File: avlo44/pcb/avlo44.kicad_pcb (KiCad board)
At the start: 2 copper layers, 356.5 x 105.3 mm, 102 parts, among them P1 OLED, SW1 SW_PUSH, SW10 SW_PUSH, SW11 SW_PUSH, SW12 SW_PUSH, SW13 SW_PUSH, SW14 SW_PUSH, SW15 SW_PUSH, SW16 SW_PUSH, SW17 SW_PUSH, SW18 SW_PUSH, SW19 SW_PUSH, SW2 SW_PUSH, SW20 SW_PUSH, SW21 SW_PUSH, SW22 SW_PUSH, SW25 SW_PUSH, SW26 SW_PUSH, SW27 SW_PUSH, SW28 SW_PUSH, SW29 SW_PUSH, SW3 SW_PUSH, SW30 SW_PUSH, SW31 SW_PUSH, SW32 SW_PUSH, SW33 SW_PUSH, SW34 SW_PUSH, SW35 SW_PUSH, SW36 SW_PUSH, SW37 SW_PUSH, SW38 SW_PUSH, SW39 SW_PUSH, SW4 SW_PUSH, SW40 SW_PUSH, SW41 SW_PUSH, SW42 SW_PUSH, SW43 SW_PUSH, SW44 SW_PUSH, SW45 SW_PUSH, SW46 SW_PUSH, SW5 SW_PUSH, SW6 SW_PUSH, SW7 SW_PUSH, SW8 SW_PUSH, SW9 SW_PUSH, U1 ProMicro

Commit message: Initial routing complete for Avlo44
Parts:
- removed L11: WS2812B, avlo-parts:WS2812B
- moved L7 4.90 mm to (317.1, -205.1)
- moved L8 2.64 mm to (331.7, -227.2)
- moved L10 1.47 mm to (272.9, -227.2)
- moved L9 0.72 mm to (310.3, -234.8)
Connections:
- L10 pad 2: Net-(L10-Pad2) -> (no net)
- SW37 pad 1: Net-(SW37-Pad1) -> col0
- SW38 pad 1: Net-(SW38-Pad1) -> col1
- SW39 pad 1: Net-(SW39-Pad1) -> col2
- SW40 pad 1: Net-(SW40-Pad1) -> col3
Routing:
- net GND: track 327.8 -> 695.8 mm, vias 12 -> 20
- net VCC: track 278.4 -> 591.0 mm, vias 8 -> 17
- net Net-(D36-Pad2): track 2.67 -> 155.0 mm, vias 0 -> 1
- net Net-(D30-Pad2): track 2.67 -> 149.1 mm, vias 0 -> 2
- net Net-(D34-Pad2): track 0.00 -> 143.0 mm, vias 0 -> 4
- net Net-(D35-Pad2): track 2.67 -> 141.7 mm, vias 0 -> 3
- net Net-(D29-Pad2): track 0.00 -> 136.4 mm, vias 0 -> 4
- net Net-(D28-Pad2): track 0.00 -> 124.6 mm, vias 0 -> 4
- net row4: track 0.00 -> 121.6 mm, vias 0 -> 2
- net Net-(D33-Pad2): track 0.00 -> 120.7 mm, vias 0 -> 4
- net Net-(L5-Pad2): track 123.4 -> 238.0 mm, vias 2 -> 4
- net Net-(D27-Pad2): track 0.00 -> 111.6 mm, vias 0 -> 4
- net Net-(D32-Pad2): track 0.00 -> 108.7 mm, vias 0 -> 4
- net row5: track 0.00 -> 106.8 mm, vias 0 -> 2
- net Net-(D26-Pad2): track 0.00 -> 95.9 mm, vias 0 -> 2
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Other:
- board size 356.5 x 105.3 mm -> 356.5 x 105.4 mm

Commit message: Add board outline for Avlo44
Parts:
- moved D1 363.1 mm to (163.1, 133.1)
- moved D10 363.1 mm to (176.8, 145.8)
- moved D11 363.1 mm to (181.4, 145.8)
- moved D12 363.1 mm to (186.0, 145.8)
- moved D13 363.1 mm to (163.1, 158.5)
- moved D14 363.1 mm to (167.7, 158.5)
- moved D15 363.1 mm to (172.3, 158.5)
- moved D16 363.1 mm to (176.8, 158.5)
- moved D17 363.1 mm to (181.4, 158.5)
- moved D18 363.1 mm to (186.0, 158.5)
- moved D19 363.1 mm to (163.1, 171.2)
- moved D2 363.1 mm to (167.7, 133.1)
- moved D20 363.1 mm to (167.7, 171.2)
- moved D21 363.1 mm to (172.3, 171.2)
- moved D22 363.1 mm to (176.8, 171.2)
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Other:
- outline, holes or cut-outs redrawn

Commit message: Update mounting holes, add artwork and add production files
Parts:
- added ?: , avlo-parts:artwork-bicyclist, F.Cu at (238.2, 195.9)
- added ?: , avlo-parts:artwork-tireswing, B.Cu at (184.5, 192.8)
- added TH1: HOLE, avlo-parts:HOLE_M2_TH, F.Cu at (63.6, 116.1)
- added TH10: HOLE, avlo-parts:HOLE_M2_TH, F.Cu at (283.9, 190.5)
- added TH11: HOLE, avlo-parts:HOLE_M2_TH, F.Cu at (211.2, 168.9)
- added TH2: HOLE, avlo-parts:HOLE_M2_TH, F.Cu at (54.8, 158.9)
- added TH3: HOLE, avlo-parts:HOLE_M2_TH, F.Cu at (129.1, 174.5)
- added TH4: HOLE, avlo-parts:HOLE_M2_TH, F.Cu at (136.2, 137.3)
- added TH5: HOLE, avlo-parts:HOLE_M2_TH, F.Cu at (358.7, 116.1)
- added TH6: HOLE, avlo-parts:HOLE_M2_TH, F.Cu at (367.4, 158.9)
- added TH7: HOLE, avlo-parts:HOLE_M2_TH, F.Cu at (293.2, 174.5)
- added TH8: HOLE, avlo-parts:HOLE_M2_TH, F.Cu at (286.0, 137.3)
- added TH9: HOLE, avlo-parts:HOLE_M2_TH, F.Cu at (138.5, 190.5)
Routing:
- net VCC: track 591.0 -> 593.6 mm
- net Net-(D30-Pad2): track 149.1 -> 150.6 mm
- net Net-(D45-Pad2): track 110.7 -> 111.5 mm
- net Net-(D46-Pad2): track 129.7 -> 130.3 mm
- net Net-(D42-Pad2): track 191.5 -> 192.2 mm
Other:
- outline, holes or cut-outs redrawn
- board text added: "Avlo44 rev 0.1"

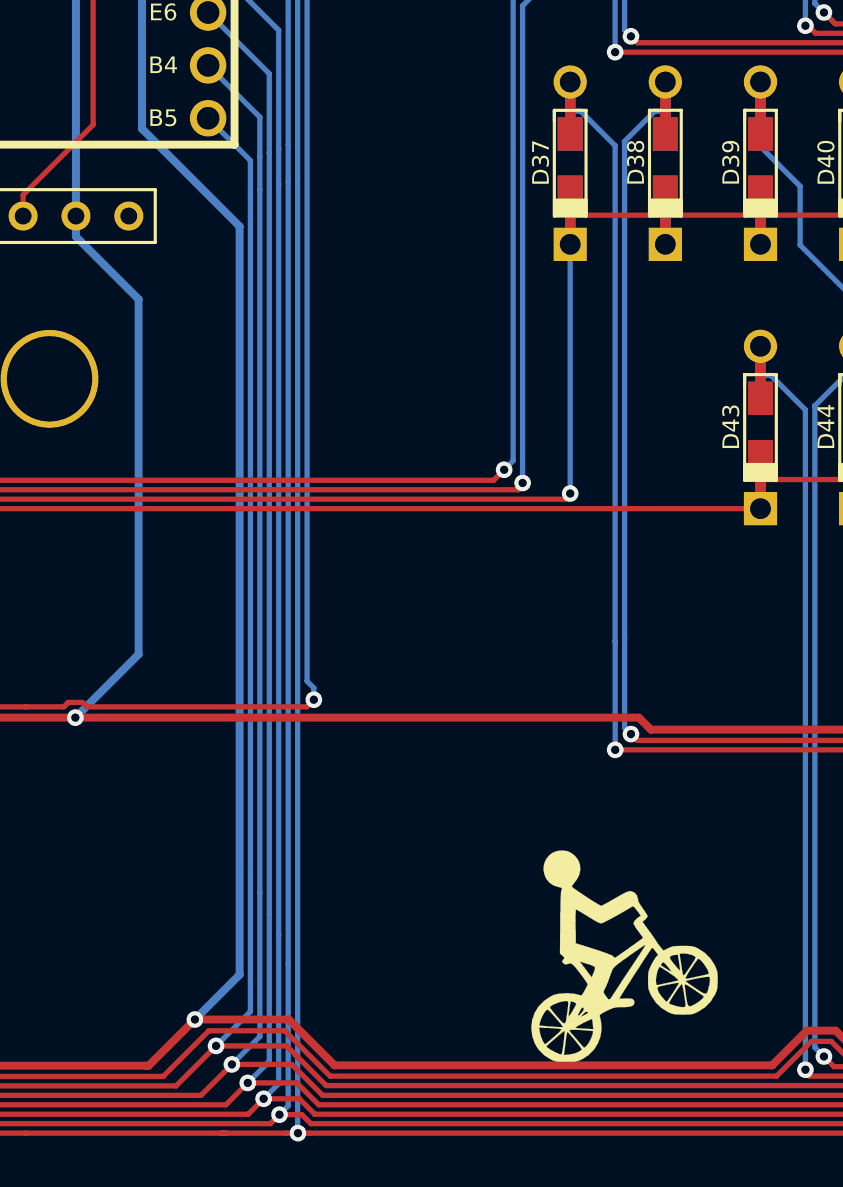
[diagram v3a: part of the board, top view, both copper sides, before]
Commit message: Fix missing trace and add switch footprint for Kailh socket
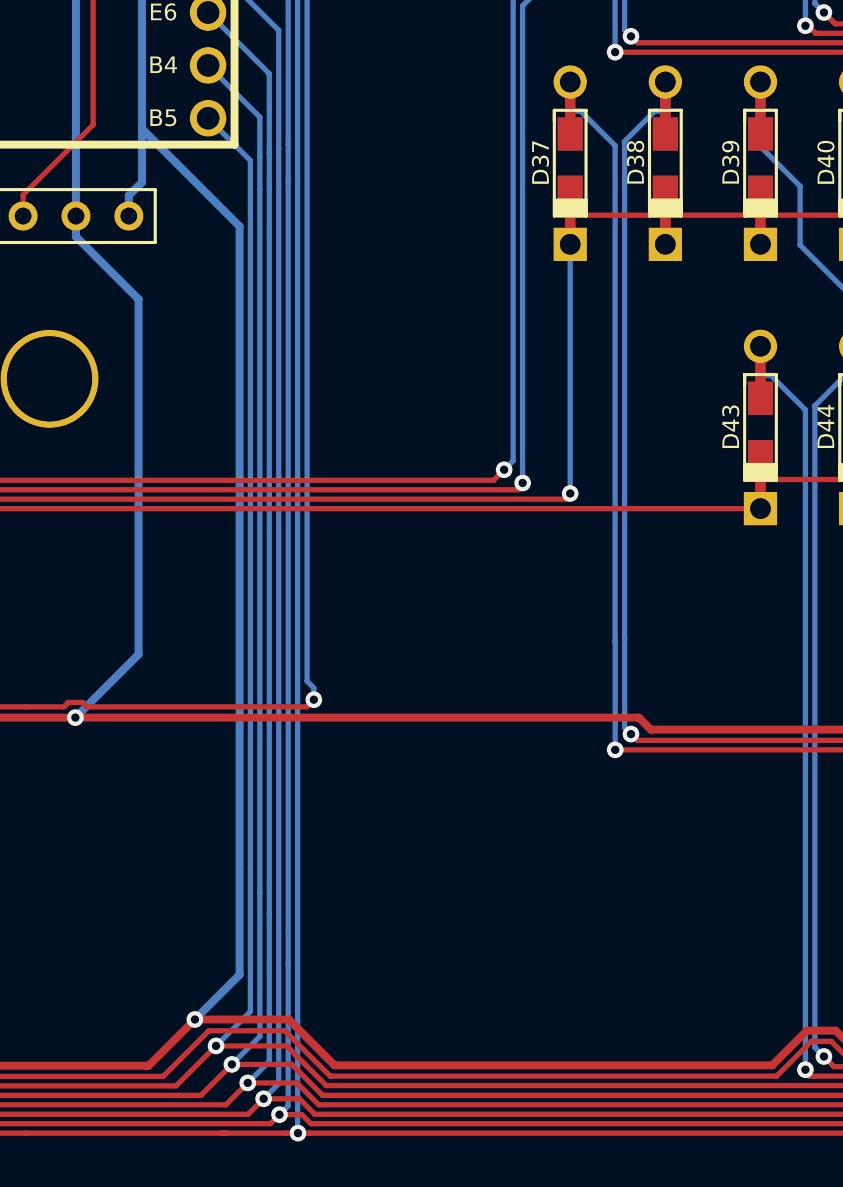
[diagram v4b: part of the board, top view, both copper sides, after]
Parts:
- removed ?: , avlo-parts:artwork-bicyclist
- removed ?: , avlo-parts:artwork-tireswing
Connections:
- P1 pad 4: (no net) -> GND
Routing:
- net GND: track 695.8 -> 700.3 mm
